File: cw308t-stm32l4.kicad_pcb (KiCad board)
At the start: 2 copper layers, 53 x 65 mm, 18 parts, among them J1 CW308T_CONNBOARD, J2 Conn_02x03_Odd_Even, U1 STM32L432KCUx

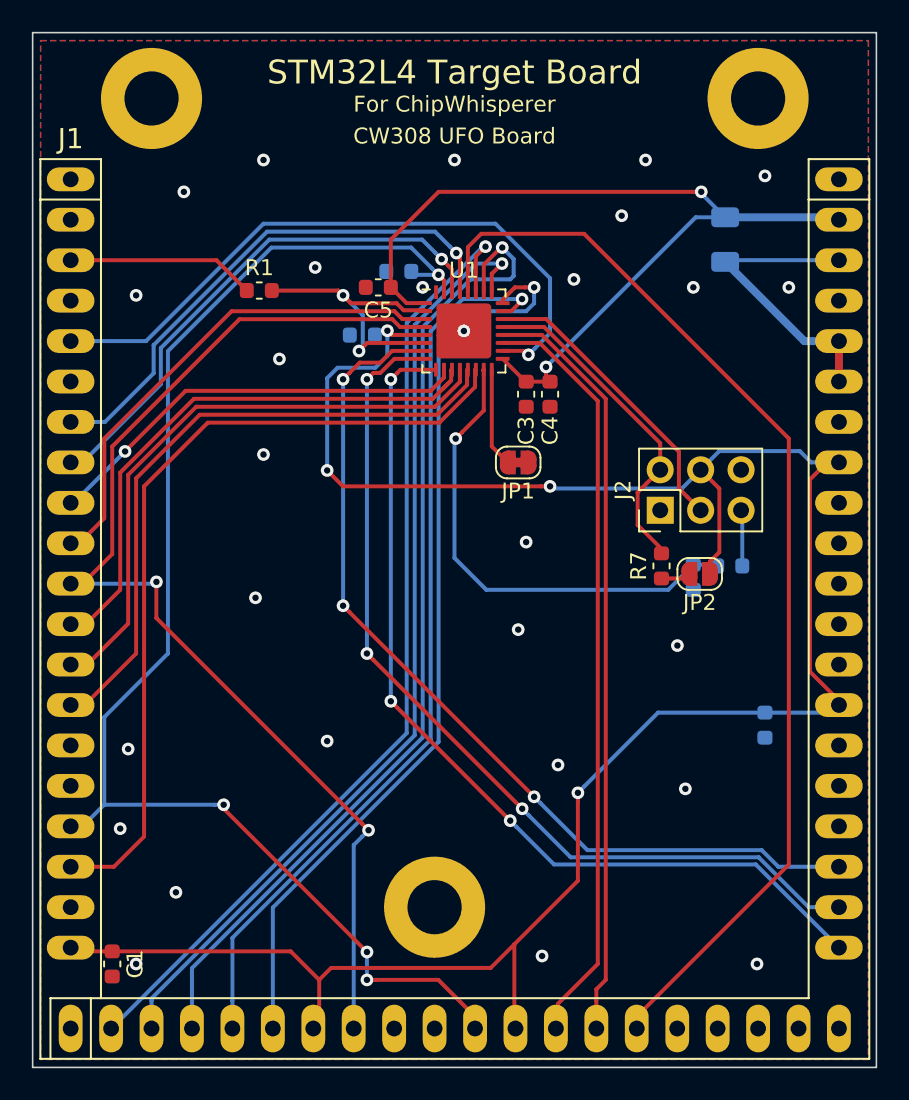
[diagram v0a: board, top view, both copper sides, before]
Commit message: Reworked with ic rotated by 90 degrees
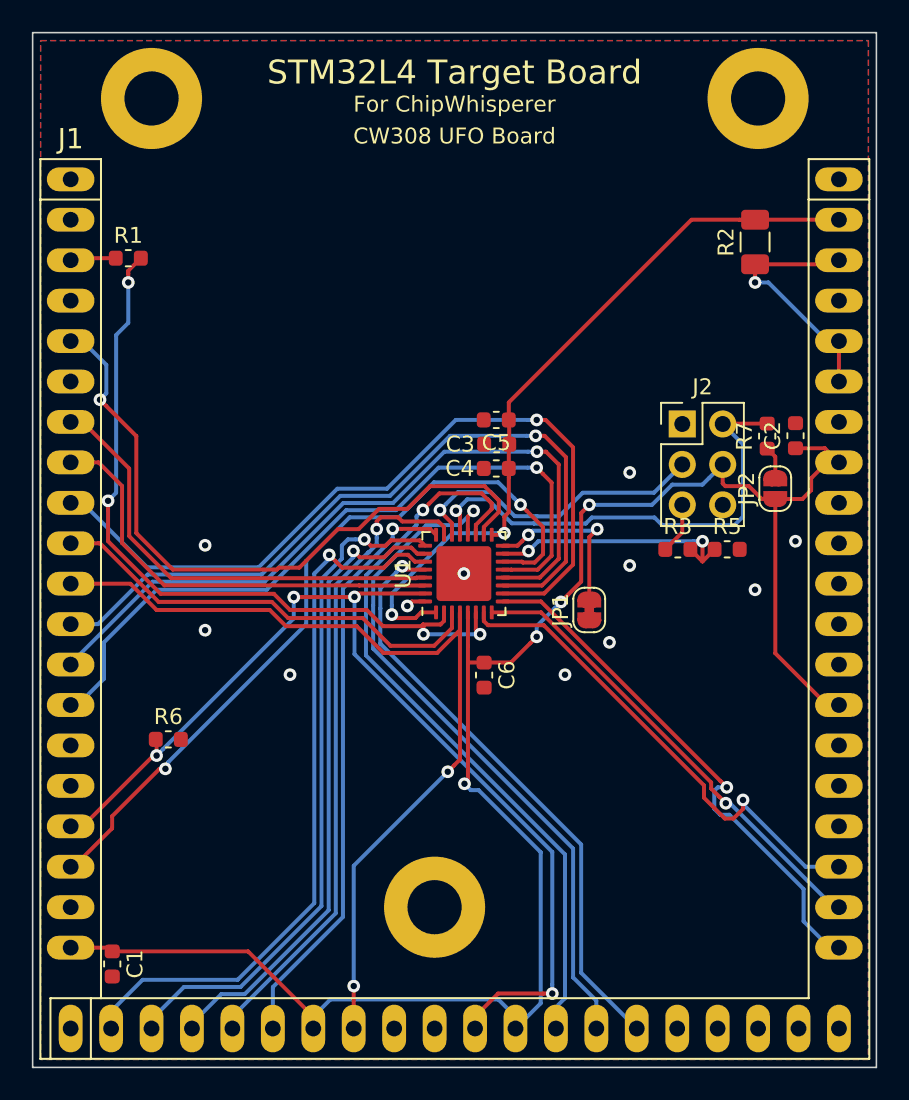
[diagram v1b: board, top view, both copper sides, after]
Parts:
- C2, C6, R2, R3, R5, R6: moved to F.Cu
- moved R6 32.8 mm to (130.0, 104.4), turned to 0 degrees
- moved C6 22.7 mm to (149.9, 100.4), turned to 270 degrees
- moved C2 18.3 mm to (169.4, 85.3), turned to 90 degrees
- moved U1 15.2 mm to (148.6, 94.0), turned to 90 degrees
- moved C5 11.1 mm to (150.6, 84.3)
- moved R7 10.5 mm to (167.6, 85.3)
- moved JP1 10.3 mm to (156.5, 96.3), turned to 90 degrees
- moved R1 8.48 mm to (127.5, 74.2)
- moved JP2 7.16 mm to (168.1, 88.6), turned to 90 degrees
- moved C4 5.76 mm to (150.6, 87.4), turned to 180 degrees
- moved J2 5.59 mm to (162.3, 84.6), turned to 0 degrees
- moved C3 3.65 mm to (150.6, 85.9), turned to 180 degrees
- moved R3 3.42 mm to (162.0, 92.5), turned to 0 degrees
- moved R5 2.76 mm to (165.1, 92.5), turned to 0 degrees
- moved R2 1.88 mm to (166.9, 73.2)
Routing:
- net /GPIO5: track 69.7 -> 37.8 mm, vias 0 -> 1
- net /CLKI: track 18.6 -> 48.3 mm, vias 2 -> 4
- net /LED2: track 57.7 -> 29.7 mm, vias 3 -> 1
- net VCC: track 141.5 -> 114.5 mm
- net /LED1: track 58.1 -> 31.1 mm, vias 3 -> 1
- net /LED3: track 57.9 -> 33.5 mm, vias 3 -> 1
- net /GPIO3: track 27.2 -> 50.3 mm
- net /TDO: track 62.5 -> 40.1 mm
- net /TCK: track 58.2 -> 37.4 mm
- net /BOOT0: track 87.7 -> 67.6 mm
- net /TDI: track 60.2 -> 43.2 mm
- net /NRST: track 73.7 -> 56.9 mm
- net /TMS: track 57.1 -> 40.7 mm
- net /TRST: track 62.1 -> 45.8 mm
- net Net-(R3-Pad2): track 30.7 -> 16.3 mm, vias 1 -> 2
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
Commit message: 2x5 pin header, minor improvements
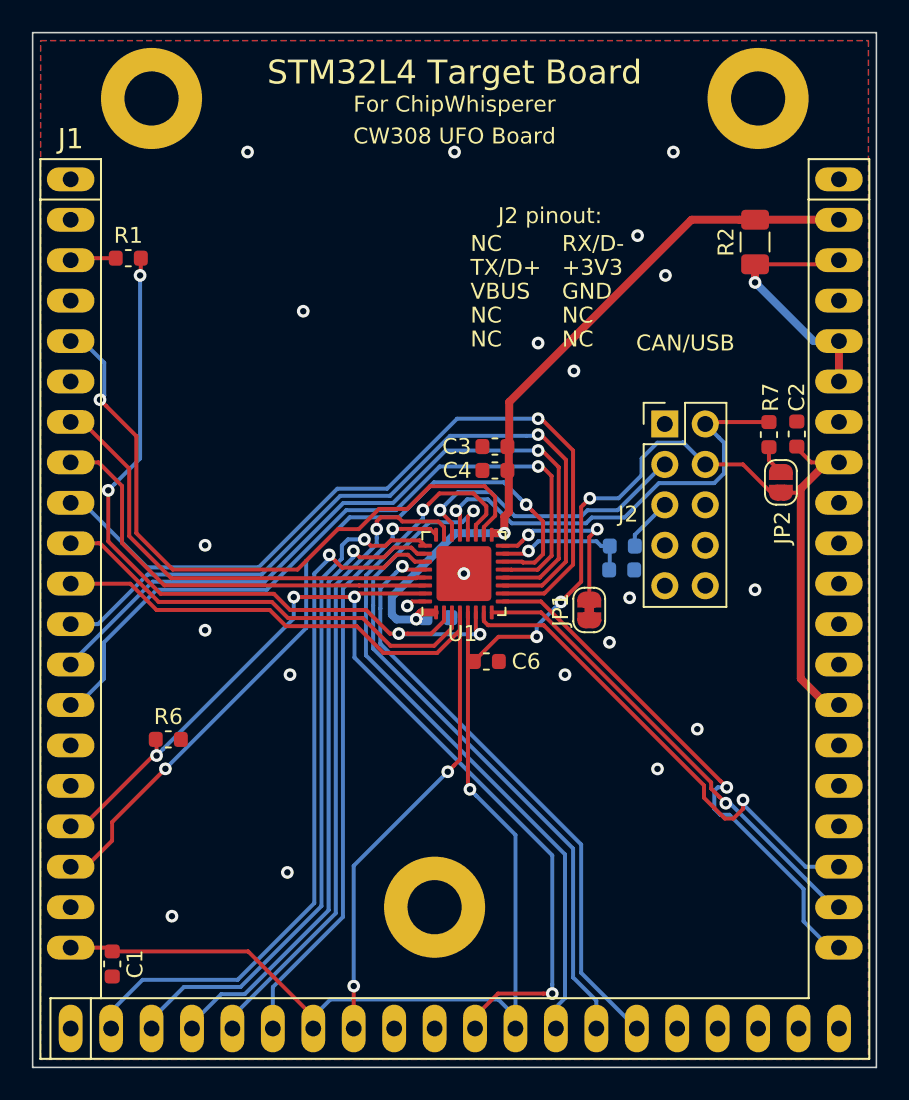
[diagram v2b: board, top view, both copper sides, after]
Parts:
- C5, R3, R5: moved to B.Cu
- J2: footprint Connector_PinHeader_2.54mm:PinHeader_2x03_P2.54mm_Vertical -> Connector_PinHeader_2.54mm:PinHeader_2x05_P2.54mm_Vertical
- moved C5 12.9 mm to (147.0, 96.8), turned to 0 degrees
- moved R5 6.75 mm to (158.5, 93.8)
- moved R3 3.50 mm to (158.5, 92.2), turned to 180 degrees
- moved J2 1.10 mm to (161.2, 84.6)
- moved C6 0.87 mm to (150.0, 99.5), turned to 0 degrees
- moved JP2 0.53 mm to (168.5, 88.2)
- moved C3 0.18 mm to (150.5, 86.0)
- moved C4 0.15 mm to (150.5, 87.5)
- moved R7 0.14 mm to (167.8, 85.2)
- moved C2 0.13 mm to (169.5, 85.2)
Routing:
- net Net-(R3-Pad2): track 16.3 -> 8.69 mm, vias 2 -> 1
- net /CAN_RX: track 30.3 -> 28.3 mm
- net /CLKI: track 48.3 -> 49.6 mm
- net /CAN_TX: track 19.5 -> 18.4 mm
- net VCC: track 114.5 -> 115.3 mm
- net Net-(C3-Pad1): track 47.6 -> 48.3 mm
- net /I2C_SCL: track 46.9 -> 46.3 mm
- net GND: vias 11 -> 21
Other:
- board text added: "+3V3"
- board text added: "CAN/USB"
- board text added: "GND"
- board text added: "J2 pinout:"
- board text added: "NC"
- board text added: "RX/D-"
- board text added: "TX/D+"
- board text added: "VBUS"

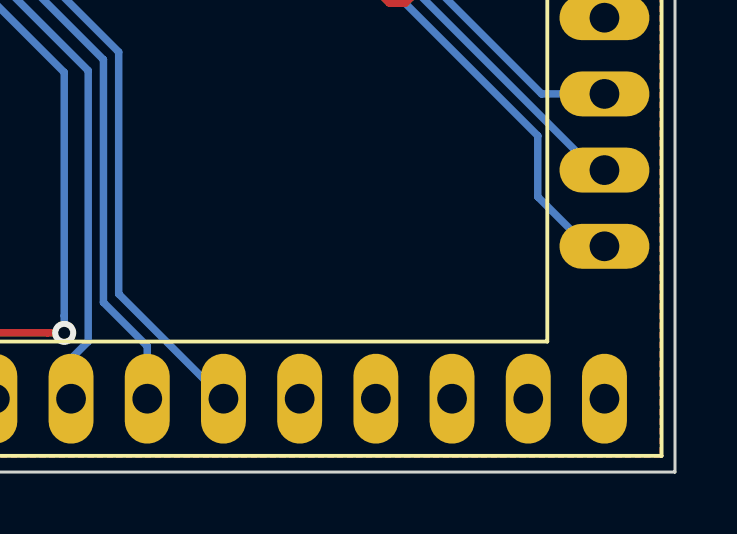
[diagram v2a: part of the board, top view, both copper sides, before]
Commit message: Add nicknames and rev to silkscreen
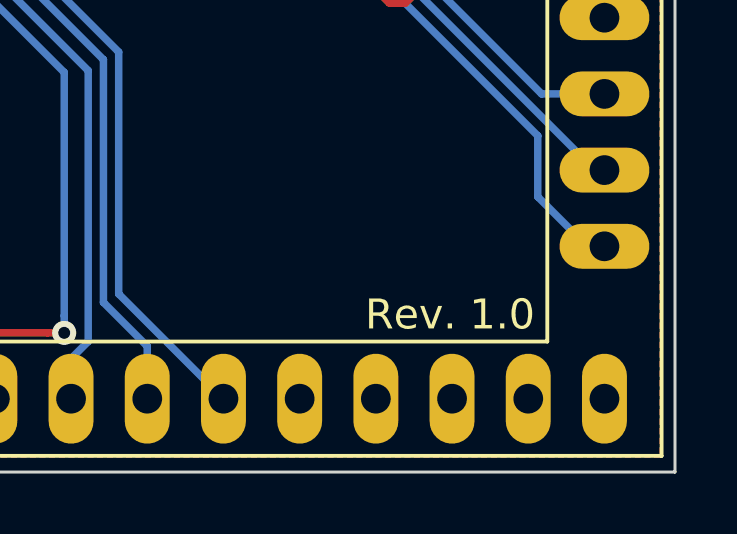
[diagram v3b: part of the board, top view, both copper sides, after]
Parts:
- moved REF** 10.2 mm to (148.0, 76.2)
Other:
- board text added: "Rev. 1.0"
- board text added: "© 2019 mickdermack, aveexy"
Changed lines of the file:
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@@
   (general
     (thickness 1.6)
-    (drawings 22)
+    (drawings 24)
     (tracks 509)
     (zones 0)
@@
   )
   (module Symbol:OSHW-Logo_5.7x6mm_SilkScreen (layer B.Cu)
-    (at 154 68 180)
+    (at 148 76.25 180)
     (descr "Open Source Hardware Logo")
     (tags "Logo OSHW")
@@
     )
   )
+  (gr_text "© 2019 mickdermack, aveexy" (at 148.25 63.25) (layer B.SilkS)
+    (effects (font (size 1 1) (thickness 0.15)) (justify mirror))
+  )
+  (gr_text "Rev. 1.0" (at 167 119.75) (layer F.SilkS)
+    (effects (font (size 1 1) (thickness 0.15)))
+  )
   (gr_text NC (at 149 79.25) (layer F.SilkS)
     (effects (font (size 1 1) (thickness 0.15)) (justify left))
@@
     (effects (font (size 1 1) (thickness 0.15)) (justify left))
   )
-  (gr_text https://github.com/mickdermack (at 148 62.5) (layer B.SilkS)
+  (gr_text https://github.com/mickdermack (at 148.25 65.5) (layer B.SilkS)
     (effects (font (size 1.1 1.1) (thickness 0.15)) (justify mirror))
   )

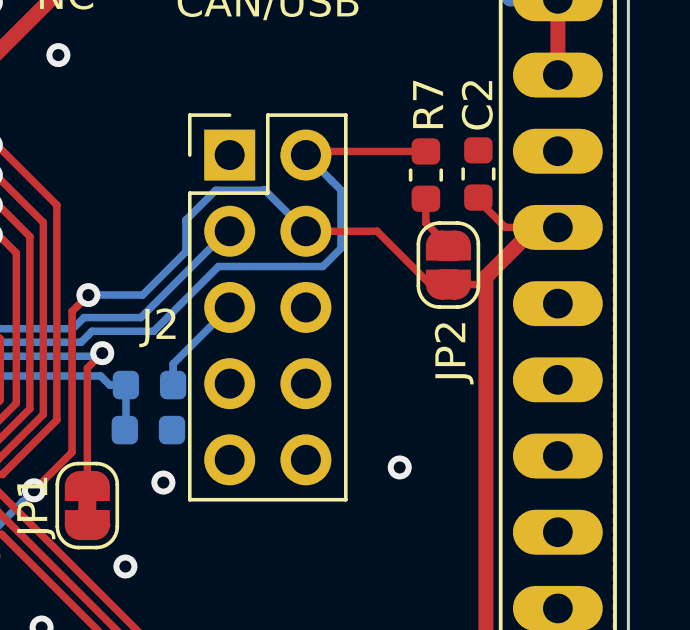
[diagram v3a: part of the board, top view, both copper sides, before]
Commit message: Moved solder pad
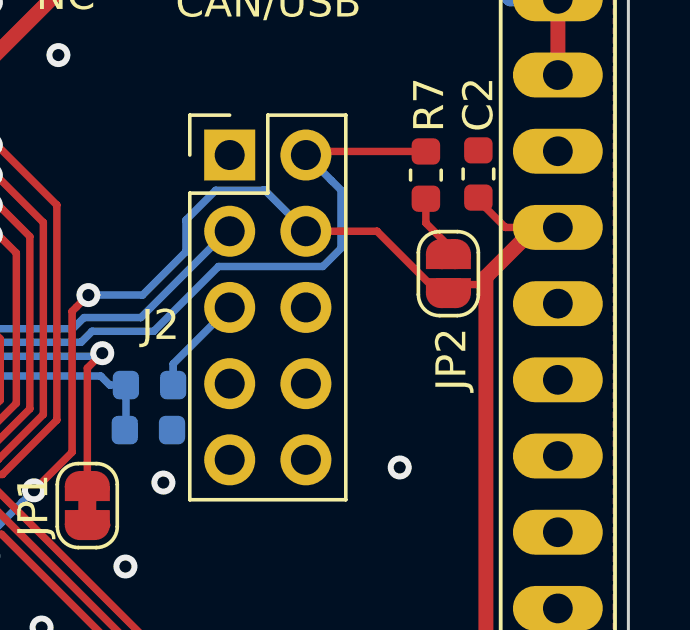
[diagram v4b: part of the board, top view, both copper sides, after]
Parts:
- moved JP2 0.28 mm to (168.5, 88.5)
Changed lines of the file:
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@@
   )
   (module Jumper:SolderJumper-2_P1.3mm_Open_RoundedPad1.0x1.5mm (layer F.Cu)
-    (at 168.5 88.25 90)
+    (at 168.5 88.534 90)
     (descr "SMD Solder Jumper, 1x1.5mm, rounded Pads, 0.3mm gap, open")
     (tags "solder jumper open")
